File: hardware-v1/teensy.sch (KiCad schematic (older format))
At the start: 31 parts, among them J1 USB-MICRO-B-SHIELDED, P4 USB_POWER, P6 CORTEX_DEBUG, SW1 PROGRAM, U7 LP38691, U8 MK20DX256VLH7, U9 MKL02Z32VFG4, X1 CRYSTAL_SMD, Y2 32kHz

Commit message: Footprint work
 - Fix ina219 footprint (for soic)
 - lm4040
 - sn65c1168e -> tssop16
 - sn74hct245 -> tsso20
 - updated bunch of caps to normal 0603 (not handsolder)
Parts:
- C10, C11, C12, C13, C26, C4, C5, C6, C7, C8, C9: footprint Capacitors_SMD:C_0603_HandSoldering -> Capacitors_SMD:C_0603
- R13, R3: footprint (none) -> Resistors_SMD:R_0603
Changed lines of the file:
@@
 $EndComp
 $Comp
-L GND #PWR44
+L GND #PWR027
 U 1 1 5658E841
 P 6850 5300
-F 0 "#PWR44" H 6850 5050 50  0001 C CNN
+F 0 "#PWR027" H 6850 5050 50  0001 C CNN
 F 1 "GND" H 6850 5150 50  0000 C CNN
 F 2 "" H 6850 5300 60  0000 C CNN
@@
 $EndComp
 $Comp
-L +3.3V #PWR40
+L +3.3V #PWR028
 U 1 1 5658ECFF
 P 1600 3450
-F 0 "#PWR40" H 1600 3300 50  0001 C CNN
+F 0 "#PWR028" H 1600 3300 50  0001 C CNN
 F 1 "+3.3V" H 1600 3590 50  0000 C CNN
 F 2 "" H 1600 3450 60  0000 C CNN
@@
 $EndComp
 $Comp
-L GND #PWR42
+L GND #PWR029
 U 1 1 5658ED8D
 P 1400 4050
-F 0 "#PWR42" H 1400 3800 50  0001 C CNN
+F 0 "#PWR029" H 1400 3800 50  0001 C CNN
 F 1 "GND" H 1400 3900 50  0000 C CNN
 F 2 "" H 1400 4050 60  0000 C CNN
@@
 $EndComp
 $Comp
-L GND #PWR43
+L GND #PWR030
 U 1 1 5658F088
 P 4100 4950
-F 0 "#PWR43" H 4100 4700 50  0001 C CNN
+F 0 "#PWR030" H 4100 4700 50  0001 C CNN
 F 1 "GND" H 4100 4800 50  0000 C CNN
 F 2 "" H 4100 4950 60  0000 C CNN
@@
 $EndComp
 $Comp
-L +3.3V #PWR45
+L +3.3V #PWR031
 U 1 1 56590BBB
 P 1600 5850
-F 0 "#PWR45" H 1600 5700 50  0001 C CNN
+F 0 "#PWR031" H 1600 5700 50  0001 C CNN
 F 1 "+3.3V" H 1600 5990 50  0000 C CNN
 F 2 "" H 1600 5850 60  0000 C CNN
@@
 NoConn ~ 1850 6300
 $Comp
-L GND #PWR35
+L GND #PWR032
 U 1 1 565927D7
 P 1700 2150
-F 0 "#PWR35" H 1700 1900 50  0001 C CNN
+F 0 "#PWR032" H 1700 1900 50  0001 C CNN
 F 1 "GND" H 1700 2000 50  0000 C CNN
 F 2 "" H 1700 2150 60  0000 C CNN
@@
 $EndComp
 $Comp
-L +3.3V #PWR30
+L +3.3V #PWR033
 U 1 1 56596469
 P 6600 1400
-F 0 "#PWR30" H 6600 1250 50  0001 C CNN
+F 0 "#PWR033" H 6600 1250 50  0001 C CNN
 F 1 "+3.3V" H 6600 1540 50  0000 C CNN
 F 2 "" H 6600 1400 60  0000 C CNN
@@
 F 0 "C10" H 6210 1670 50  0000 L CNN
 F 1 "2.2uF" H 6210 1520 50  0000 L CNN
-F 2 "Capacitors_SMD:C_0603_HandSoldering" H 6200 1600 60  0001 C CNN
+F 2 "Capacitors_SMD:C_0603" H 6200 1600 60  0001 C CNN
 F 3 "" H 6200 1600 60  0000 C CNN
 	1    6200 1600
@@
 F 0 "C9" H 6010 1670 50  0000 L CNN
 F 1 ".1uF" H 6010 1520 50  0000 L CNN
-F 2 "Capacitors_SMD:C_0603_HandSoldering" H 6000 1600 60  0001 C CNN
+F 2 "Capacitors_SMD:C_0603" H 6000 1600 60  0001 C CNN
 F 3 "" H 6000 1600 60  0000 C CNN
 	1    6000 1600
@@
 F 0 "C8" H 5810 1670 50  0000 L CNN
 F 1 ".1uF" H 5810 1520 50  0000 L CNN
-F 2 "Capacitors_SMD:C_0603_HandSoldering" H 5800 1600 60  0001 C CNN
+F 2 "Capacitors_SMD:C_0603" H 5800 1600 60  0001 C CNN
 F 3 "" H 5800 1600 60  0000 C CNN
 	1    5800 1600
@@
 F 0 "C7" H 5610 1670 50  0000 L CNN
 F 1 ".1uF" H 5610 1520 50  0000 L CNN
-F 2 "Capacitors_SMD:C_0603_HandSoldering" H 5600 1600 60  0001 C CNN
+F 2 "Capacitors_SMD:C_0603" H 5600 1600 60  0001 C CNN
 F 3 "" H 5600 1600 60  0000 C CNN
 	1    5600 1600
@@
 $EndComp
 $Comp
-L GND #PWR34
+L GND #PWR034
 U 1 1 565968B4
 P 5900 1900
-F 0 "#PWR34" H 5900 1650 50  0001 C CNN
+F 0 "#PWR034" H 5900 1650 50  0001 C CNN
 F 1 "GND" H 5900 1750 50  0000 C CNN
 F 2 "" H 5900 1900 60  0000 C CNN
@@
 $EndComp
 $Comp
-L GND #PWR37
+L GND #PWR035
 U 1 1 56598327
 P 5300 3300
-F 0 "#PWR37" H 5300 3050 50  0001 C CNN
+F 0 "#PWR035" H 5300 3050 50  0001 C CNN
 F 1 "GND" H 5300 3150 50  0000 C CNN
 F 2 "" H 5300 3300 60  0000 C CNN
@@
 F 0 "C12" H 6460 2620 50  0000 L CNN
 F 1 ".1uF" H 6460 2470 50  0000 L CNN
-F 2 "Capacitors_SMD:C_0603_HandSoldering" H 6450 2550 60  0001 C CNN
+F 2 "Capacitors_SMD:C_0603" H 6450 2550 60  0001 C CNN
 F 3 "" H 6450 2550 60  0000 C CNN
 	1    6450 2550
@@
 F 0 "C11" H 5410 2620 50  0000 L CNN
 F 1 ".1uF" H 5410 2470 50  0000 L CNN
-F 2 "Capacitors_SMD:C_0603_HandSoldering" H 5400 2550 60  0001 C CNN
+F 2 "Capacitors_SMD:C_0603" H 5400 2550 60  0001 C CNN
 F 3 "" H 5400 2550 60  0000 C CNN
 	1    5400 2550
@@
 $EndComp
 $Comp
-L GND #PWR32
+L GND #PWR036
 U 1 1 565A6A4F
 P 3550 1700
-F 0 "#PWR32" H 3550 1450 50  0001 C CNN
+F 0 "#PWR036" H 3550 1450 50  0001 C CNN
 F 1 "GND" H 3550 1550 50  0000 C CNN
 F 2 "" H 3550 1700 60  0000 C CNN
@@
 $EndComp
 $Comp
-L +5V #PWR28
+L +5V #PWR037
 U 1 1 565A6A86
 P 2900 1250
-F 0 "#PWR28" H 2900 1100 50  0001 C CNN
+F 0 "#PWR037" H 2900 1100 50  0001 C CNN
 F 1 "+5V" H 2900 1390 50  0000 C CNN
 F 2 "" H 2900 1250 60  0000 C CNN
@@
 	3950 1350 4250 1350
 $Comp
-L +3.3V #PWR29
+L +3.3V #PWR038
 U 1 1 565A6D4A
 P 4250 1250
-F 0 "#PWR29" H 4250 1100 50  0001 C CNN
+F 0 "#PWR038" H 4250 1100 50  0001 C CNN
 F 1 "+3.3V" H 4250 1390 50  0000 C CNN
 F 2 "" H 4250 1250 60  0000 C CNN
@@
 F 0 "C6" H 4110 1620 50  0000 L CNN
 F 1 "2.2uF" H 4110 1470 50  0000 L CNN
-F 2 "Capacitors_SMD:C_0603_HandSoldering" H 4100 1550 60  0001 C CNN
+F 2 "Capacitors_SMD:C_0603" H 4100 1550 60  0001 C CNN
 F 3 "" H 4100 1550 60  0000 C CNN
 	1    4100 1550
@@
 	3550 1600 3550 1700
 $Comp
-L GND #PWR33
+L GND #PWR039
 U 1 1 565A70D1
 P 4100 1700
-F 0 "#PWR33" H 4100 1450 50  0001 C CNN
+F 0 "#PWR039" H 4100 1450 50  0001 C CNN
 F 1 "GND" H 4100 1550 50  0000 C CNN
 F 2 "" H 4100 1700 60  0000 C CNN
@@
 F 0 "C5" H 3010 1620 50  0000 L CNN
 F 1 "2.2uF" H 3010 1470 50  0000 L CNN
-F 2 "Capacitors_SMD:C_0603_HandSoldering" H 3000 1550 60  0001 C CNN
+F 2 "Capacitors_SMD:C_0603" H 3000 1550 60  0001 C CNN
 F 3 "" H 3000 1550 60  0000 C CNN
 	1    3000 1550
@@
 	3000 1650 3000 1700
 $Comp
-L GND #PWR31
+L GND #PWR040
 U 1 1 565AC891
 P 3000 1700
-F 0 "#PWR31" H 3000 1450 50  0001 C CNN
+F 0 "#PWR040" H 3000 1450 50  0001 C CNN
 F 1 "GND" H 3000 1550 50  0000 C CNN
 F 2 "" H 3000 1700 60  0000 C CNN
@@
 $EndComp
 $Comp
-L +5V #PWR26
+L +5V #PWR041
 U 1 1 565AEF07
 P 2300 750
-F 0 "#PWR26" H 2300 600 50  0001 C CNN
+F 0 "#PWR041" H 2300 600 50  0001 C CNN
 F 1 "+5V" H 2300 890 50  0000 C CNN
 F 2 "" H 2300 750 60  0000 C CNN
@@
 F 0 "C4" H 1510 1120 50  0000 L CNN
 F 1 "2.2uF" H 1510 970 50  0000 L CNN
-F 2 "Capacitors_SMD:C_0603_HandSoldering" H 1500 1050 60  0001 C CNN
+F 2 "Capacitors_SMD:C_0603" H 1500 1050 60  0001 C CNN
 F 3 "" H 1500 1050 60  0000 C CNN
 	1    1500 1050
@@
 $EndComp
 $Comp
-L GND #PWR27
+L GND #PWR042
 U 1 1 565B08A1
 P 1500 1150
-F 0 "#PWR27" H 1500 900 50  0001 C CNN
+F 0 "#PWR042" H 1500 900 50  0001 C CNN
 F 1 "GND" H 1500 1000 50  0000 C CNN
 F 2 "" H 1500 1150 60  0000 C CNN
@@
 	8250 2450 8600 2450
 $Comp
-L GND #PWR36
+L GND #PWR043
 U 1 1 565BDF2E
 P 10200 2600
-F 0 "#PWR36" H 10200 2350 50  0001 C CNN
+F 0 "#PWR043" H 10200 2350 50  0001 C CNN
 F 1 "GND" H 10200 2450 50  0000 C CNN
 F 2 "" H 10200 2600 60  0000 C CNN
@@
 NoConn ~ 1800 4300
 $Comp
-L +3.3V #PWR38
+L +3.3V #PWR044
 U 1 1 567B1DAE
 P 5750 3300
-F 0 "#PWR38" H 5750 3150 50  0001 C CNN
+F 0 "#PWR044" H 5750 3150 50  0001 C CNN
 F 1 "+3.3V" H 5750 3440 50  0000 C CNN
 F 2 "" H 5750 3300 60  0000 C CNN
@@
 F 0 "C13" H 5760 3570 50  0000 L CNN
 F 1 ".1uF" H 5760 3420 50  0000 L CNN
-F 2 "Capacitors_SMD:C_0603_HandSoldering" H 5750 3500 60  0001 C CNN
+F 2 "Capacitors_SMD:C_0603" H 5750 3500 60  0001 C CNN
 F 3 "" H 5750 3500 60  0000 C CNN
 	1    5750 3500
@@
 Connection ~ 5750 3350
 $Comp
-L GND #PWR41
+L GND #PWR045
 U 1 1 567B220D
 P 5750 3650
-F 0 "#PWR41" H 5750 3400 50  0001 C CNN
+F 0 "#PWR045" H 5750 3400 50  0001 C CNN
 F 1 "GND" H 5750 3500 50  0000 C CNN
 F 2 "" H 5750 3650 60  0000 C CNN
@@
 Connection ~ 5200 2250
 $Comp
-L PWR_FLAG #FLG2
+L PWR_FLAG #FLG046
 U 1 1 567B5BB9
 P 5550 2200
-F 0 "#FLG2" H 5550 2295 50  0001 C CNN
+F 0 "#FLG046" H 5550 2295 50  0001 C CNN
 F 1 "PWR_FLAG" H 5550 2380 50  0000 C CNN
 F 2 "" H 5550 2200 60  0000 C CNN
@@
 	6600 3200 6600 3300
 $Comp
-L GND #PWR39
+L GND #PWR047
 U 1 1 568579A5
 P 6600 3300
-F 0 "#PWR39" H 6600 3050 50  0001 C CNN
+F 0 "#PWR047" H 6600 3050 50  0001 C CNN
 F 1 "GND" H 6600 3150 50  0000 C CNN
 F 2 "" H 6600 3300 60  0000 C CNN
@@
 Connection ~ 1600 6150
 $Comp
-L GND #PWR46
+L GND #PWR048
 U 1 1 56858A76
 P 1100 6250
-F 0 "#PWR46" H 1100 6000 50  0001 C CNN
+F 0 "#PWR048" H 1100 6000 50  0001 C CNN
 F 1 "GND" H 1100 6100 50  0000 C CNN
 F 2 "" H 1100 6250 60  0000 C CNN
@@
 F 0 "C26" H 1360 3820 50  0000 L CNN
 F 1 ".1uF" H 1360 3670 50  0000 L CNN
-F 2 "Capacitors_SMD:C_0603_HandSoldering" H 1350 3750 60  0001 C CNN
+F 2 "Capacitors_SMD:C_0603" H 1350 3750 60  0001 C CNN
 F 3 "" H 1350 3750 60  0000 C CNN
 	1    1350 3750
@@
 F 0 "R3" V 3330 3600 50  0000 C CNN
 F 1 "0" V 3250 3600 50  0000 C CNN
-F 2 "" V 3180 3600 50  0000 C CNN
+F 2 "Resistors_SMD:R_0603" V 3180 3600 50  0001 C CNN
 F 3 "" H 3250 3600 50  0000 C CNN
 	1    3250 3600
@@
 F 0 "D7" H 6050 2650 50  0000 C CNN
 F 1 "LM4040QCEM3-3.0/NOPB" H 6050 2450 50  0000 C CNN
-F 2 "" H 6050 2550 50  0000 C CNN
+F 2 "" H 6050 2550 50  0001 C CNN
 F 3 "" H 6050 2550 50  0000 C CNN
 	1    6050 2550
@@
 F 0 "R13" V 3430 4550 50  0000 C CNN
 F 1 "0 DNP" V 3350 4550 50  0000 C CNN
-F 2 "" V 3280 4550 50  0000 C CNN
+F 2 "Resistors_SMD:R_0603" V 3280 4550 50  0001 C CNN
 F 3 "" H 3350 4550 50  0000 C CNN
 	1    3350 4550

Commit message: fix tl2575
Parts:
- D7: footprint (none) -> TO_SOT_Packages_SMD:SOT-23
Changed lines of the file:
@@
 F 0 "D7" H 6050 2650 50  0000 C CNN
 F 1 "LM4040QCEM3-3.0/NOPB" H 6050 2450 50  0000 C CNN
-F 2 "" H 6050 2550 50  0001 C CNN
+F 2 "TO_SOT_Packages_SMD:SOT-23" H 6050 2550 50  0001 C CNN
 F 3 "" H 6050 2550 50  0000 C CNN
 	1    6050 2550

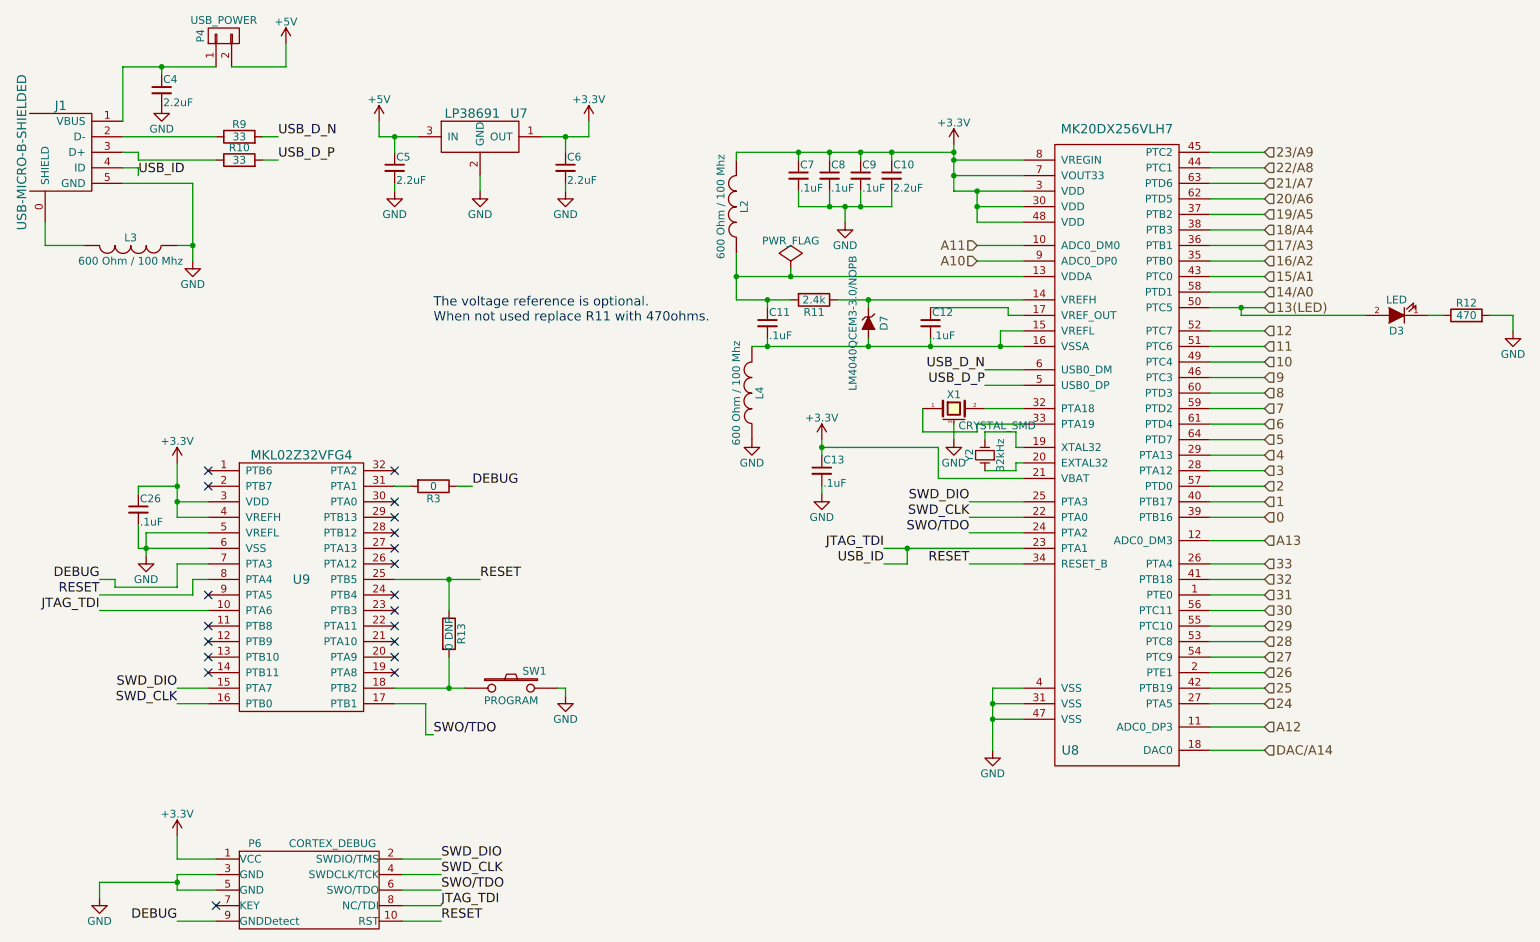
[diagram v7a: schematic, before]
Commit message: First draft of revision B
Lots of changes to the board. Almost completely re-layed out.

Will do some verification now.
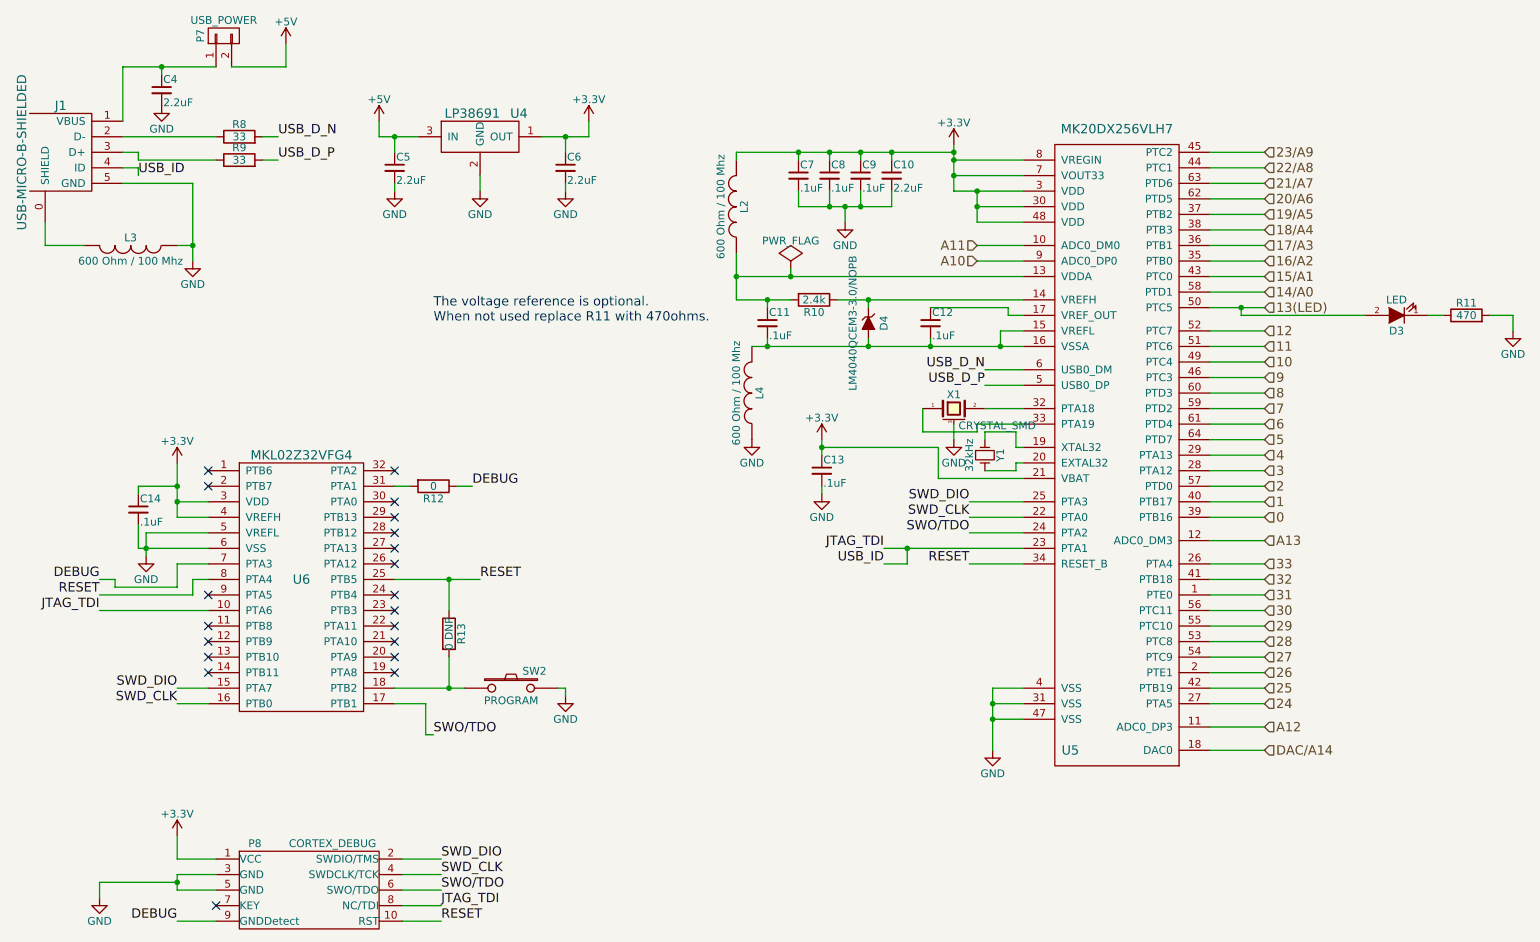
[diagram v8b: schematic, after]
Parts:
- D3: footprint LEDs:LED-0603 -> LEDs:LED_0603
- L2, L3, L4: footprint Resistors_SMD:R_0603_HandSoldering -> Resistors_SMD:R_0603
- R10: renamed from R11; footprint Resistors_SMD:R_0603_HandSoldering -> Resistors_SMD:R_0603
- R11: renamed from R12; footprint Resistors_SMD:R_0603_HandSoldering -> Resistors_SMD:R_0603
- R8: renamed from R9; footprint Resistors_SMD:R_0603_HandSoldering -> Resistors_SMD:R_0603
- R9: renamed from R10; footprint Resistors_SMD:R_0603_HandSoldering -> Resistors_SMD:R_0603
- renumbered C26 to C14, D7 to D4, P4 to P7, P6 to P8, R3 to R12, SW1 to SW2, U7 to U4, U8 to U5, U9 to U6, Y2 to Y1
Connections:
- net at U5.19 (XTAL32): now also Y1.1; no longer Y1.2
- net at U5.20 (EXTAL32): now also Y1.2; no longer Y1.1
